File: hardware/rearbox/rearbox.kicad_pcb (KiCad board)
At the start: 4 copper layers, 120 x 60 mm, 7 parts

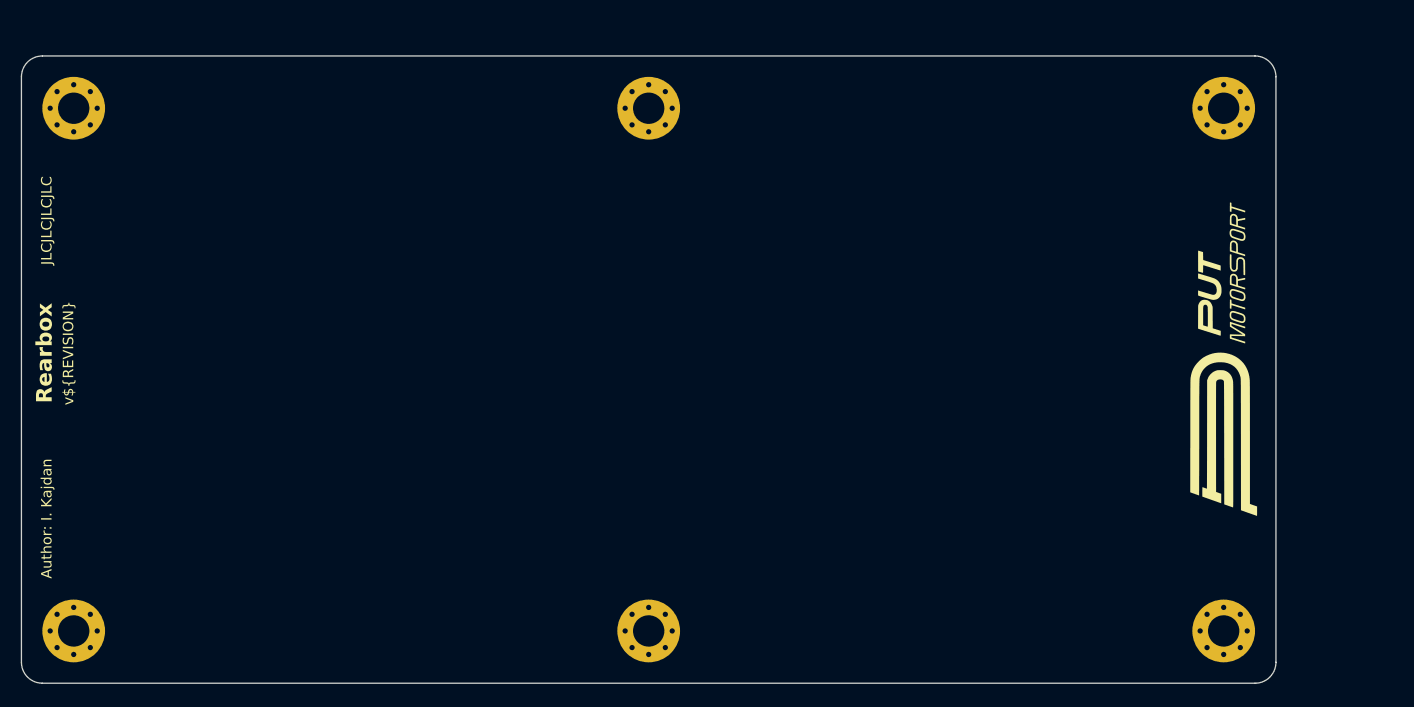
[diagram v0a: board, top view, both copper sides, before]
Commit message: Place components on the PCB
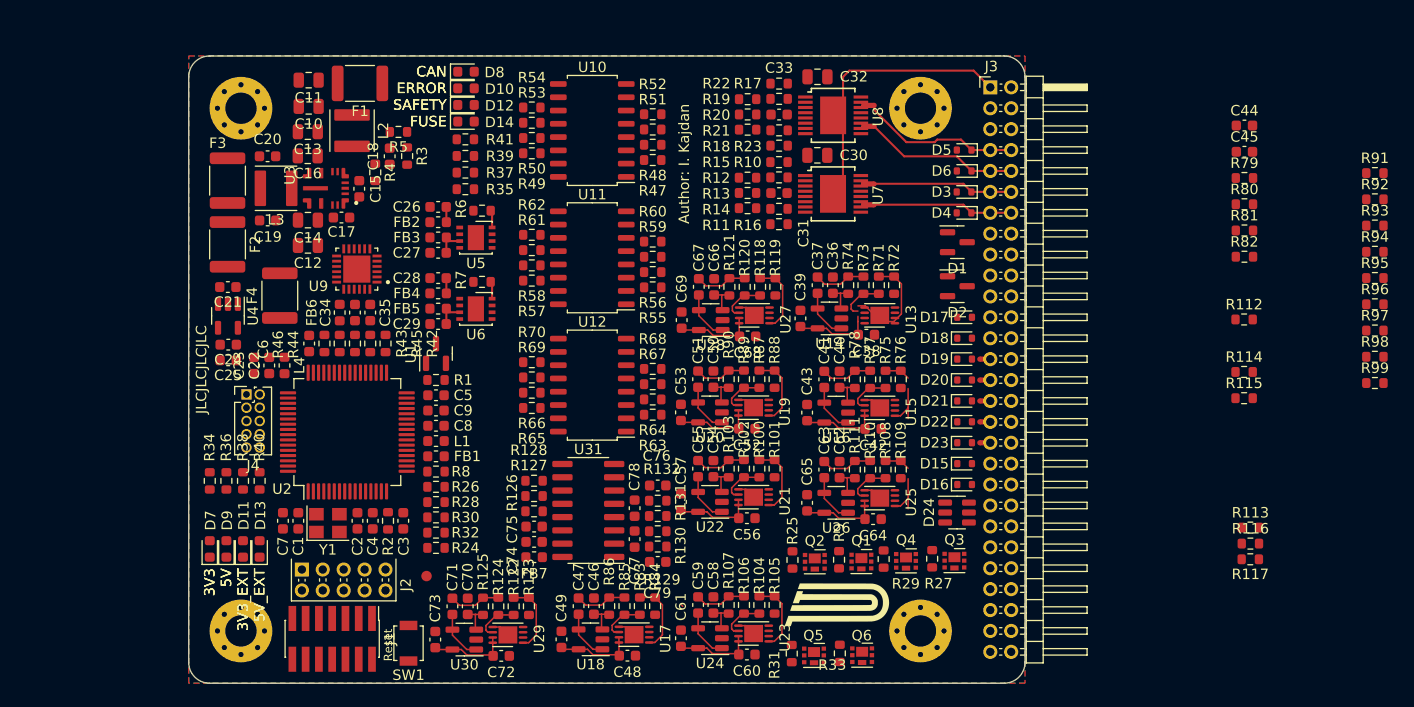
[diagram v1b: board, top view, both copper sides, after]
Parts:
- removed the REF** at (148.0, 129.0)
- removed the REF** at (148.0, 79.0)
- added C1: 10p, Capacitor_SMD:C_0603_1608Metric, F.Cu at (114.5, 118.5)
- added C10: 2u2, Capacitor_SMD:C_0805_2012Metric, F.Cu at (115.5, 78.8)
- added C11: 2u2, Capacitor_SMD:C_0805_2012Metric, F.Cu at (115.5, 76.3)
- added C12: 4u7, Capacitor_SMD:C_0805_2012Metric, F.Cu at (115.4, 92.1)
- added C13: 4u7, Capacitor_SMD:C_0805_2012Metric, F.Cu at (115.4, 81.2)
- added C14: 220n, Capacitor_SMD:C_0805_2012Metric, F.Cu at (115.4, 89.7)
- added C15: 1u, Capacitor_SMD:C_0603_1608Metric, F.Cu at (120.3, 86.7)
- added C16: 220n, Capacitor_SMD:C_0805_2012Metric, F.Cu at (115.4, 83.6)
- added C17: 100n, Capacitor_SMD:C_0603_1608Metric, F.Cu at (118.6, 89.5)
- added C18: 22p, Capacitor_SMD:C_0603_1608Metric, F.Cu at (123.2, 83.6)
- added C19: 22u, Capacitor_SMD:C_0603_1608Metric, F.Cu at (111.6, 89.7)
- added C2: 10p, Capacitor_SMD:C_0603_1608Metric, F.Cu at (120.1, 118.5)
- added C20: 22u, Capacitor_SMD:C_0603_1608Metric, F.Cu at (111.5, 83.6)
- added C21: 1u, Capacitor_SMD:C_0603_1608Metric, F.Cu at (107.7, 96.1)
- added C22: 1u, Capacitor_SMD:C_0603_1608Metric, F.Cu at (111.7, 103.6)
- added C23: 100n, Capacitor_SMD:C_0603_1608Metric, F.Cu at (110.2, 103.6)
- added C24: 100n, Capacitor_SMD:C_0603_1608Metric, F.Cu at (107.8, 101.6)
- added C25: 1u, Capacitor_SMD:C_0603_1608Metric, F.Cu at (107.8, 103.1)
- added C26: 100n, Capacitor_SMD:C_0603_1608Metric, F.Cu at (127.9, 88.4)
- added C27: 100n, Capacitor_SMD:C_0603_1608Metric, F.Cu at (127.9, 92.8)
- added C28: 100n, Capacitor_SMD:C_0603_1608Metric, F.Cu at (127.9, 95.2)
- added C29: 100n, Capacitor_SMD:C_0603_1608Metric, F.Cu at (127.9, 99.6)
- added C3: 100n, Capacitor_SMD:C_0603_1608Metric, F.Cu at (124.5, 118.5)
- added C30: 100n, Capacitor_SMD:C_0805_2012Metric, F.Cu at (164.1, 83.5)
- added C31: 10n, Capacitor_SMD:C_0603_1608Metric, F.Cu at (160.5, 87.1)
- added C32: 100n, Capacitor_SMD:C_0805_2012Metric, F.Cu at (164.1, 76.0)
- added C33: 10n, Capacitor_SMD:C_0603_1608Metric, F.Cu at (160.5, 79.6)
- added C34: 1u, Capacitor_SMD:C_0603_1608Metric, F.Cu at (119.9, 98.5)
- added C35: 100n, Capacitor_SMD:C_0603_1608Metric, F.Cu at (121.4, 98.5)
- added C36: 100n, Capacitor_SMD:C_0603_1608Metric, F.Cu at (165.6, 95.9)
- added C37: 100n, Capacitor_SMD:C_0603_1608Metric, F.Cu at (164.2, 95.9)
- added C38: 100n, Capacitor_SMD:C_0603_1608Metric, F.Cu at (168.8, 100.7)
- added C39: 100n, Capacitor_SMD:C_0603_1608Metric, F.Cu at (162.5, 99.1)
- added C4: 100n, Capacitor_SMD:C_0603_1608Metric, F.Cu at (121.6, 118.5)
- added C40: 100n, Capacitor_SMD:C_0603_1608Metric, F.Cu at (166.3, 104.9)
- added C41: 100n, Capacitor_SMD:C_0603_1608Metric, F.Cu at (164.8, 104.9)
- added C42: 100n, Capacitor_SMD:C_0603_1608Metric, F.Cu at (169.5, 109.7)
- added C43: 100n, Capacitor_SMD:C_0603_1608Metric, F.Cu at (163.2, 108.1)
- added C44: 10n, Capacitor_SMD:C_0603_1608Metric, F.Cu at (205.0, 80.7)
- added C45: 10n, Capacitor_SMD:C_0603_1608Metric, F.Cu at (205.0, 83.2)
- added C46: 100n, Capacitor_SMD:C_0603_1608Metric, F.Cu at (142.8, 126.6)
- added C47: 100n, Capacitor_SMD:C_0603_1608Metric, F.Cu at (141.3, 126.6)
- added C48: 100n, Capacitor_SMD:C_0603_1608Metric, F.Cu at (146.0, 131.4)
- added C49: 100n, Capacitor_SMD:C_0603_1608Metric, F.Cu at (139.7, 129.8)
- added C5: 100n, Capacitor_SMD:C_0603_1608Metric, F.Cu at (127.7, 106.5)
- added C50: 100n, Capacitor_SMD:C_0603_1608Metric, F.Cu at (154.2, 104.9)
- added C51: 100n, Capacitor_SMD:C_0603_1608Metric, F.Cu at (152.7, 104.9)
- added C52: 100n, Capacitor_SMD:C_0603_1608Metric, F.Cu at (157.4, 109.7)
- added C53: 100n, Capacitor_SMD:C_0603_1608Metric, F.Cu at (151.1, 108.1)
- added C54: 100n, Capacitor_SMD:C_0603_1608Metric, F.Cu at (154.2, 113.5)
- added C55: 100n, Capacitor_SMD:C_0603_1608Metric, F.Cu at (152.7, 113.5)
- added C56: 100n, Capacitor_SMD:C_0603_1608Metric, F.Cu at (157.4, 118.2)
- added C57: 100n, Capacitor_SMD:C_0603_1608Metric, F.Cu at (151.1, 116.7)
- added C58: 100n, Capacitor_SMD:C_0603_1608Metric, F.Cu at (154.2, 126.5)
- added C59: 100n, Capacitor_SMD:C_0603_1608Metric, F.Cu at (152.7, 126.5)
- added C6: 100n, Capacitor_SMD:C_0603_1608Metric, F.Cu at (115.5, 101.5)
- added C60: 100n, Capacitor_SMD:C_0603_1608Metric, F.Cu at (157.4, 131.3)
- added C61: 100n, Capacitor_SMD:C_0603_1608Metric, F.Cu at (151.1, 129.7)
- added C62: 100n, Capacitor_SMD:C_0603_1608Metric, F.Cu at (166.3, 113.6)
- added C63: 100n, Capacitor_SMD:C_0603_1608Metric, F.Cu at (164.8, 113.6)
- added C64: 100n, Capacitor_SMD:C_0603_1608Metric, F.Cu at (169.5, 118.3)
- added C65: 100n, Capacitor_SMD:C_0603_1608Metric, F.Cu at (163.2, 116.7)
- added C66: 100n, Capacitor_SMD:C_0603_1608Metric, F.Cu at (154.3, 96.1)
- added C67: 100n, Capacitor_SMD:C_0603_1608Metric, F.Cu at (152.8, 96.1)
- added C68: 100n, Capacitor_SMD:C_0603_1608Metric, F.Cu at (157.5, 100.8)
- added C69: 100n, Capacitor_SMD:C_0603_1608Metric, F.Cu at (151.2, 99.3)
- added C7: 100n, Capacitor_SMD:C_0603_1608Metric, F.Cu at (113.0, 118.5)
- added C70: 100n, Capacitor_SMD:C_0603_1608Metric, F.Cu at (130.7, 126.6)
- added C71: 100n, Capacitor_SMD:C_0603_1608Metric, F.Cu at (129.2, 126.6)
- added C72: 100n, Capacitor_SMD:C_0603_1608Metric, F.Cu at (133.9, 131.4)
- added C73: 100n, Capacitor_SMD:C_0603_1608Metric, F.Cu at (127.6, 129.8)
- added C74: 1u, Capacitor_SMD:C_0603_1608Metric, F.Cu at (137.0, 120.5)
- added C75: 100n, Capacitor_SMD:C_0603_1608Metric, F.Cu at (137.0, 119.0)
- added C76: 100n, Capacitor_SMD:C_0603_1608Metric, F.Cu at (148.9, 115.1)
- added C77: 100n, Capacitor_SMD:C_0603_1608Metric, F.Cu at (146.7, 120.2)
- added C78: 100n, Capacitor_SMD:C_0603_1608Metric, F.Cu at (146.7, 117.3)
- added C79: 1u, Capacitor_SMD:C_0603_1608Metric, F.Cu at (148.9, 122.4)
- added C8: 1u, Capacitor_SMD:C_0603_1608Metric, F.Cu at (127.7, 109.4)
- added C9: 100n, Capacitor_SMD:C_0603_1608Metric, F.Cu at (127.7, 107.9)
- added D1: PESD2CAN, Package_TO_SOT_SMD:SOT-23, F.Cu at (177.5, 91.8)
- added D10: Red, LED_SMD:LED_0603_1608Metric, F.Cu at (130.5, 77.1)
- added D11: Green, LED_SMD:LED_0603_1608Metric, F.Cu at (109.2, 121.2)
- added D12: Red, LED_SMD:LED_0603_1608Metric, F.Cu at (130.5, 78.7)
- added D13: Green, LED_SMD:LED_0603_1608Metric, F.Cu at (110.8, 121.2)
- added D14: Red, LED_SMD:LED_0603_1608Metric, F.Cu at (130.5, 80.3)
- added D15: 5V, Diode_SMD:D_SOD-523, F.Cu at (178.2, 113.0)
- added D16: 5V, Diode_SMD:D_SOD-523, F.Cu at (178.2, 115.0)
- added D17: 5V, Diode_SMD:D_SOD-523, F.Cu at (178.2, 99.0)
- added D18: 5V, Diode_SMD:D_SOD-523, F.Cu at (178.2, 101.0)
- added D19: 5V, Diode_SMD:D_SOD-523, F.Cu at (178.2, 103.0)
- added D2: PESD2CAN, Package_TO_SOT_SMD:SOT-23, F.Cu at (177.5, 96.0)
- added D20: 5V, Diode_SMD:D_SOD-523, F.Cu at (178.2, 105.0)
- added D21: 5V, Diode_SMD:D_SOD-523, F.Cu at (178.2, 107.0)
- added D22: 5V, Diode_SMD:D_SOD-523, F.Cu at (178.2, 109.0)
- added D23: 5V, Diode_SMD:D_SOD-523, F.Cu at (178.2, 111.0)
- added D24: CPDT6-5V4, Package_TO_SOT_SMD:SOT-23-6, F.Cu at (177.5, 117.7)
- added D3: PMEG3010EB, Diode_SMD:D_SOD-523, F.Cu at (178.2, 87.0)
- added D4: PMEG3010EB, Diode_SMD:D_SOD-523, F.Cu at (178.2, 89.0)
- added D5: PMEG3010EB, Diode_SMD:D_SOD-523, F.Cu at (178.2, 83.0)
- added D6: PMEG3010EB, Diode_SMD:D_SOD-523, F.Cu at (178.2, 85.0)
- added D7: Green, LED_SMD:LED_0603_1608Metric, F.Cu at (106.0, 121.2)
- added D8: Red, LED_SMD:LED_0603_1608Metric, F.Cu at (130.5, 75.5)
- added D9: Green, LED_SMD:LED_0603_1608Metric, F.Cu at (107.6, 121.2)
- added F1: 1.5A, Fuse:Fuse_1812_4532Metric, F.Cu at (120.4, 76.6)
- added F2: 500mA, Fuse:Fuse_1812_4532Metric, F.Cu at (107.7, 92.0)
- added F3: 200mA, Fuse:Fuse_1812_4532Metric, F.Cu at (107.7, 85.9)
- added F4: 100mA, Fuse:Fuse_1812_4532Metric, F.Cu at (112.7, 96.9)
- added FB1: 470R, Inductor_SMD:L_0603_1608Metric, F.Cu at (127.7, 112.3)
- added FB2: 470R, Inductor_SMD:L_0603_1608Metric, F.Cu at (127.9, 89.9)
- added FB3: 470R, Inductor_SMD:L_0603_1608Metric, F.Cu at (127.9, 91.4)
- added FB4: 470R, Inductor_SMD:L_0603_1608Metric, F.Cu at (127.9, 96.7)
- added FB5: 470R, Inductor_SMD:L_0603_1608Metric, F.Cu at (127.9, 98.2)
- added FB6: 470R, Inductor_SMD:L_0603_1608Metric, F.Cu at (118.4, 98.5)
- added FB7: 470R, Inductor_SMD:L_0603_1608Metric, F.Cu at (137.0, 121.9)
- added G***: LOGO, Local_Library:PUTM_Logo_10mm, F.Cu at (166.0, 126.5)
- added G***: LOGO, Local_Library:PUTM_Signature_Box_15mm, B.Cu at (152.4, 106.0)
- added J1: STDC14, Connector_PinHeader_1.27mm:PinHeader_2x07_P1.27mm_Vertical_SMD, F.Cu at (117.7, 129.8)
- added J2: ST-LINK, Local_Library:STLINK-V3MINIE, F.Cu at (114.8, 125.1)
- added J3: Conn_02x28_Top_Bottom, Connector_PinHeader_2.00mm:PinHeader_2x28_P2.00mm_Horizontal, F.Cu at (180.7, 77.0)
- added J4: Auxiliary, Connector_PinHeader_1.27mm:PinHeader_2x05_P1.27mm_Vertical, F.Cu at (109.5, 106.4)
- added L1: 10u, Inductor_SMD:L_0603_1608Metric, F.Cu at (127.7, 110.8)
- added L2: 1u5, Inductor_SMD:L_Abracon_ASPI-4030S, F.Cu at (119.6, 81.1)
- added L3: 1u5, Inductor_SMD:L_Abracon_ASPI-4030S, F.Cu at (112.4, 86.7)
- added L4: 10u, Inductor_SMD:L_0603_1608Metric, F.Cu at (113.2, 103.6)
- added NT1: NetTie_2, NetTie:NetTie-2_SMD_Pad0.5mm, F.Cu at (169.1, 86.2)
- added NT2: NetTie_2, NetTie:NetTie-2_SMD_Pad0.5mm, F.Cu at (169.1, 88.2)
- added NT3: NetTie_2, NetTie:NetTie-2_SMD_Pad0.5mm, F.Cu at (169.1, 78.7)
- added NT4: NetTie_2, NetTie:NetTie-2_SMD_Pad0.5mm, F.Cu at (169.1, 80.7)
- added NT5: NetTie_2, NetTie:NetTie-2_SMD_Pad0.5mm, F.Cu at (180.2, 103.0)
- added NT6: NetTie_2, NetTie:NetTie-2_SMD_Pad0.5mm, F.Cu at (180.2, 105.0)
- added NT7: NetTie_2, NetTie:NetTie-2_SMD_Pad0.5mm, F.Cu at (180.2, 107.0)
- added NT8: NetTie_2, NetTie:NetTie-2_SMD_Pad0.5mm, F.Cu at (180.2, 109.0)
- added NT9: NetTie_2, NetTie:NetTie-2_SMD_Pad0.5mm, F.Cu at (180.2, 111.0)
- added Q1: BUK6D210, Package_DFN_QFN:Diodes_UDFN2020-6_Type-F, F.Cu at (168.3, 122.4)
- added Q2: BUK6D210, Package_DFN_QFN:Diodes_UDFN2020-6_Type-F, F.Cu at (163.9, 122.4)
- added Q3: BUK6D210, Package_DFN_QFN:Diodes_UDFN2020-6_Type-F, F.Cu at (177.2, 122.3)
- added Q4: BUK6D210, Package_DFN_QFN:Diodes_UDFN2020-6_Type-F, F.Cu at (172.6, 122.3)
- added Q5: BUK6D210, Package_DFN_QFN:Diodes_UDFN2020-6_Type-F, F.Cu at (163.8, 131.3)
- added Q6: BUK6D210, Package_DFN_QFN:Diodes_UDFN2020-6_Type-F, F.Cu at (168.4, 131.3)
- added R1: 1k, Resistor_SMD:R_0603_1608Metric, F.Cu at (127.7, 105.0)
- added R10: 100R, Resistor_SMD:R_0603_1608Metric, F.Cu at (160.5, 84.2)
- added R100: TBD, Resistor_SMD:R_0603_1608Metric, F.Cu at (158.6, 113.5)
- added R101: TBD, Resistor_SMD:R_0603_1608Metric, F.Cu at (160.0, 113.5)
- added R102: 3k3, Resistor_SMD:R_0603_1608Metric, F.Cu at (157.1, 113.5)
- added R103: 3k3, Resistor_SMD:R_0603_1608Metric, F.Cu at (155.7, 113.5)
- added R104: TBD, Resistor_SMD:R_0603_1608Metric, F.Cu at (158.6, 126.5)
- added R105: TBD, Resistor_SMD:R_0603_1608Metric, F.Cu at (160.0, 126.5)
- added R106: 3k3, Resistor_SMD:R_0603_1608Metric, F.Cu at (157.1, 126.5)
- added R107: 3k3, Resistor_SMD:R_0603_1608Metric, F.Cu at (155.7, 126.5)
- added R108: TBD, Resistor_SMD:R_0603_1608Metric, F.Cu at (170.7, 113.6)
- added R109: TBD, Resistor_SMD:R_0603_1608Metric, F.Cu at (172.1, 113.6)
- added R11: 100R, Resistor_SMD:R_0603_1608Metric, F.Cu at (160.5, 90.1)
- added R110: 3k3, Resistor_SMD:R_0603_1608Metric, F.Cu at (169.2, 113.6)
- added R111: 3k3, Resistor_SMD:R_0603_1608Metric, F.Cu at (167.7, 113.6)
- added R112: 50k, Resistor_SMD:R_0603_1608Metric, F.Cu at (205.0, 99.2)
- added R113: 50k, Resistor_SMD:R_0603_1608Metric, F.Cu at (205.6, 119.1)
- added R114: 50k, Resistor_SMD:R_0603_1608Metric, F.Cu at (205.0, 104.2)
- added R115: 5k, Resistor_SMD:R_0603_1608Metric, F.Cu at (205.0, 106.7)
- added R116: 50k, Resistor_SMD:R_0603_1608Metric, F.Cu at (205.6, 120.6)
- added R117: 5k, Resistor_SMD:R_0603_1608Metric, F.Cu at (205.5, 122.1)
- added R118: TBD, Resistor_SMD:R_0603_1608Metric, F.Cu at (158.7, 96.1)
- added R119: TBD, Resistor_SMD:R_0603_1608Metric, F.Cu at (160.1, 96.1)
- added R12: 100R, Resistor_SMD:R_0603_1608Metric, F.Cu at (157.5, 85.6)
- added R120: 3k3, Resistor_SMD:R_0603_1608Metric, F.Cu at (157.2, 96.1)
- added R121: 3k3, Resistor_SMD:R_0603_1608Metric, F.Cu at (155.7, 96.1)
- added R122: TBD, Resistor_SMD:R_0603_1608Metric, F.Cu at (135.1, 126.6)
- added R123: TBD, Resistor_SMD:R_0603_1608Metric, F.Cu at (136.5, 126.6)
- added R124: 3k3, Resistor_SMD:R_0603_1608Metric, F.Cu at (133.6, 126.6)
- added R125: 3k3, Resistor_SMD:R_0603_1608Metric, F.Cu at (132.2, 126.6)
- added R126: 100R, Resistor_SMD:R_0603_1608Metric, F.Cu at (137.0, 117.6)
- added R127: 100R, Resistor_SMD:R_0603_1608Metric, F.Cu at (137.0, 116.1)
- added R128: 100R, Resistor_SMD:R_0603_1608Metric, F.Cu at (137.0, 114.6)
- added R129: 51R, Resistor_SMD:R_0603_1608Metric, F.Cu at (148.9, 120.9)
- added R13: 100R, Resistor_SMD:R_0603_1608Metric, F.Cu at (157.5, 87.1)
- added R130: 51R, Resistor_SMD:R_0603_1608Metric, F.Cu at (148.9, 119.5)
- added R131: 51R, Resistor_SMD:R_0603_1608Metric, F.Cu at (148.9, 118.0)
- added R132: 51R, Resistor_SMD:R_0603_1608Metric, F.Cu at (148.9, 116.5)
- added R14: 100R, Resistor_SMD:R_0603_1608Metric, F.Cu at (157.5, 88.6)
- added R15: 15k, Resistor_SMD:R_0603_1608Metric, F.Cu at (160.5, 85.6)
- added R16: TBD, Resistor_SMD:R_0603_1608Metric, F.Cu at (160.5, 88.6)
- added R17: 100R, Resistor_SMD:R_0603_1608Metric, F.Cu at (160.5, 76.6)
- added R18: 100R, Resistor_SMD:R_0603_1608Metric, F.Cu at (160.5, 82.6)
- added R19: 100R, Resistor_SMD:R_0603_1608Metric, F.Cu at (157.5, 78.1)
- added R2: 10k, Resistor_SMD:R_0603_1608Metric, F.Cu at (123.1, 118.5)
- added R20: 100R, Resistor_SMD:R_0603_1608Metric, F.Cu at (157.5, 79.6)
- added R21: 100R, Resistor_SMD:R_0603_1608Metric, F.Cu at (157.5, 81.0)
- added R22: 15k, Resistor_SMD:R_0603_1608Metric, F.Cu at (160.5, 78.1)
- added R23: TBD, Resistor_SMD:R_0603_1608Metric, F.Cu at (160.5, 81.1)
- added R24: 100R, Resistor_SMD:R_0603_1608Metric, F.Cu at (127.7, 121.1)
- added R25: 10k, Resistor_SMD:R_0603_1608Metric, F.Cu at (161.8, 122.2)
- added R26: 100R, Resistor_SMD:R_0603_1608Metric, F.Cu at (127.7, 115.2)
- added R27: 10k, Resistor_SMD:R_0603_1608Metric, F.Cu at (175.1, 122.1)
- added R28: 100R, Resistor_SMD:R_0603_1608Metric, F.Cu at (127.7, 116.7)
- added R29: 10k, Resistor_SMD:R_0603_1608Metric, F.Cu at (170.5, 122.1)
- added R3: 100k, Resistor_SMD:R_0603_1608Metric, F.Cu at (124.9, 83.6)
- added R30: 100R, Resistor_SMD:R_0603_1608Metric, F.Cu at (127.7, 118.1)
- added R31: 10k, Resistor_SMD:R_0603_1608Metric, F.Cu at (161.7, 131.2)
- added R32: 100R, Resistor_SMD:R_0603_1608Metric, F.Cu at (127.7, 119.6)
- added R33: 10k, Resistor_SMD:R_0603_1608Metric, F.Cu at (166.3, 131.1)
- added R34: 82R, Resistor_SMD:R_0603_1608Metric, F.Cu at (106.0, 114.6)
- added R35: 120R, Resistor_SMD:R_0603_1608Metric, F.Cu at (130.5, 86.7)
- added R36: 270R, Resistor_SMD:R_0603_1608Metric, F.Cu at (107.6, 114.6)
- added R37: 120R, Resistor_SMD:R_0603_1608Metric, F.Cu at (130.5, 85.2)
- added R38: 82R, Resistor_SMD:R_0603_1608Metric, F.Cu at (109.2, 114.6)
- added R39: 120R, Resistor_SMD:R_0603_1608Metric, F.Cu at (130.5, 83.6)
- added R4: 24k9, Resistor_SMD:R_0603_1608Metric, F.Cu at (121.8, 85.1)
- added R40: 270R, Resistor_SMD:R_0603_1608Metric, F.Cu at (110.8, 114.6)
- added R41: 120R, Resistor_SMD:R_0603_1608Metric, F.Cu at (130.5, 82.0)
- added R42: 100R, Resistor_SMD:R_0603_1608Metric, F.Cu at (122.8, 101.5)
- added R43: 100R, Resistor_SMD:R_0603_1608Metric, F.Cu at (119.9, 101.5)
- added R44: 100R, Resistor_SMD:R_0603_1608Metric, F.Cu at (118.4, 101.5)
- added R45: 100R, Resistor_SMD:R_0603_1608Metric, F.Cu at (121.4, 101.5)
- added R46: 0R, Resistor_SMD:R_0603_1608Metric, F.Cu at (117.0, 101.5)
- added R47: 2k, Resistor_SMD:R_0603_1608Metric, F.Cu at (148.4, 84.0)
- added R48: 2k, Resistor_SMD:R_0603_1608Metric, F.Cu at (148.4, 82.5)
- added R49: 10k, Resistor_SMD:R_0603_1608Metric, F.Cu at (136.8, 83.3)
- added R5: 1k, Resistor_SMD:R_0603_1608Metric, F.Cu at (124.1, 81.3)
- added R50: 10k, Resistor_SMD:R_0603_1608Metric, F.Cu at (136.8, 81.8)
- added R51: 2k, Resistor_SMD:R_0603_1608Metric, F.Cu at (148.4, 81.0)
- added R52: 2k, Resistor_SMD:R_0603_1608Metric, F.Cu at (148.4, 79.6)
- added R53: 10k, Resistor_SMD:R_0603_1608Metric, F.Cu at (136.8, 80.4)
- added R54: 10k, Resistor_SMD:R_0603_1608Metric, F.Cu at (136.8, 78.9)
- added R55: 2k, Resistor_SMD:R_0603_1608Metric, F.Cu at (148.4, 96.1)
- added R56: 2k, Resistor_SMD:R_0603_1608Metric, F.Cu at (148.4, 94.7)
- added R57: 10k, Resistor_SMD:R_0603_1608Metric, F.Cu at (136.8, 95.5)
- added R58: 10k, Resistor_SMD:R_0603_1608Metric, F.Cu at (136.8, 94.0)
- added R59: 2k, Resistor_SMD:R_0603_1608Metric, F.Cu at (148.4, 93.2)
- added R6: 0R, Resistor_SMD:R_0603_1608Metric, F.Cu at (132.1, 88.8)
- added R60: 2k, Resistor_SMD:R_0603_1608Metric, F.Cu at (148.4, 91.8)
- added R61: 10k, Resistor_SMD:R_0603_1608Metric, F.Cu at (136.8, 92.6)
- added R62: 10k, Resistor_SMD:R_0603_1608Metric, F.Cu at (136.8, 91.1)
- added R63: 2k, Resistor_SMD:R_0603_1608Metric, F.Cu at (148.4, 108.3)
- added R64: 2k, Resistor_SMD:R_0603_1608Metric, F.Cu at (148.4, 106.9)
- added R65: 10k, Resistor_SMD:R_0603_1608Metric, F.Cu at (136.8, 107.7)
- added R66: 10k, Resistor_SMD:R_0603_1608Metric, F.Cu at (136.8, 106.2)
- added R67: 2k, Resistor_SMD:R_0603_1608Metric, F.Cu at (148.4, 105.4)
- added R68: 2k, Resistor_SMD:R_0603_1608Metric, F.Cu at (148.4, 103.9)
- added R69: 10k, Resistor_SMD:R_0603_1608Metric, F.Cu at (136.8, 104.8)
- added R7: 0R, Resistor_SMD:R_0603_1608Metric, F.Cu at (132.1, 95.6)
- added R70: 10k, Resistor_SMD:R_0603_1608Metric, F.Cu at (136.8, 103.3)
- added R71: TBD, Resistor_SMD:R_0603_1608Metric, F.Cu at (170.0, 95.9)
- added R72: TBD, Resistor_SMD:R_0603_1608Metric, F.Cu at (171.5, 95.9)
- added R73: 3k3, Resistor_SMD:R_0603_1608Metric, F.Cu at (168.5, 95.9)
- added R74: 3k3, Resistor_SMD:R_0603_1608Metric, F.Cu at (167.1, 95.9)
- added R75: TBD, Resistor_SMD:R_0603_1608Metric, F.Cu at (170.7, 104.9)
- added R76: TBD, Resistor_SMD:R_0603_1608Metric, F.Cu at (172.1, 104.9)
- added R77: 3k3, Resistor_SMD:R_0603_1608Metric, F.Cu at (169.2, 104.9)
- added R78: 3k3, Resistor_SMD:R_0603_1608Metric, F.Cu at (167.7, 104.9)
- added R79: 560R, Resistor_SMD:R_0603_1608Metric, F.Cu at (205.0, 85.7)
- added R8: 100R, Resistor_SMD:R_0603_1608Metric, F.Cu at (127.7, 113.8)
- added R80: 100R, Resistor_SMD:R_0603_1608Metric, F.Cu at (205.0, 88.2)
- added R81: 560R, Resistor_SMD:R_0603_1608Metric, F.Cu at (205.0, 90.7)
- added R82: 100R, Resistor_SMD:R_0603_1608Metric, F.Cu at (205.0, 93.2)
- added R83: TBD, Resistor_SMD:R_0603_1608Metric, F.Cu at (147.2, 126.6)
- added R84: TBD, Resistor_SMD:R_0603_1608Metric, F.Cu at (148.6, 126.6)
- added R85: 3k3, Resistor_SMD:R_0603_1608Metric, F.Cu at (145.7, 126.6)
- added R86: 3k3, Resistor_SMD:R_0603_1608Metric, F.Cu at (144.2, 126.6)
- added R87: TBD, Resistor_SMD:R_0603_1608Metric, F.Cu at (158.6, 104.9)
- added R88: TBD, Resistor_SMD:R_0603_1608Metric, F.Cu at (160.0, 104.9)
- added R89: 3k3, Resistor_SMD:R_0603_1608Metric, F.Cu at (157.1, 104.9)
- added R9: 10k, Resistor_SMD:R_0603_1608Metric, F.Cu at (166.2, 122.2)
- added R90: 3k3, Resistor_SMD:R_0603_1608Metric, F.Cu at (155.7, 104.9)
- added R91: 1k, Resistor_SMD:R_0603_1608Metric, F.Cu at (217.5, 85.2)
- added R92: 1k, Resistor_SMD:R_0603_1608Metric, F.Cu at (217.5, 87.7)
- added R93: 1k, Resistor_SMD:R_0603_1608Metric, F.Cu at (217.5, 90.2)
- added R94: 1k, Resistor_SMD:R_0603_1608Metric, F.Cu at (217.5, 92.7)
- added R95: 3k, Resistor_SMD:R_0603_1608Metric, F.Cu at (217.5, 95.2)
- added R96: 1k, Resistor_SMD:R_0603_1608Metric, F.Cu at (217.5, 97.8)
- added R97: 3k, Resistor_SMD:R_0603_1608Metric, F.Cu at (217.5, 100.3)
- added R98: 1k, Resistor_SMD:R_0603_1608Metric, F.Cu at (217.5, 102.8)
- added R99: 3k, Resistor_SMD:R_0603_1608Metric, F.Cu at (217.5, 105.3)
- added REF**: Fiducial_1mm_Mask2mm, Fiducial:Fiducial_1mm_Mask2mm, F.Cu at (126.8, 123.8)
- added SW1: Reset, Button_Switch_SMD:SW_SPST_B3U-1000P, F.Cu at (125.0, 130.2)
- added U1: LM4040C33FTA, Package_TO_SOT_SMD:SOT-23, F.Cu at (127.7, 102.5)
- added U10: TLP291-4, Package_SO:SOIC-16_4.55x10.3mm_P1.27mm, F.Cu at (142.6, 81.1)
- added U11: TLP291-4, Package_SO:SOIC-16_4.55x10.3mm_P1.27mm, F.Cu at (142.6, 93.3)
- added U12: TLP291-4, Package_SO:SOIC-16_4.55x10.3mm_P1.27mm, F.Cu at (142.6, 105.5)
- added U13: MCP6N11-005, Package_DFN_QFN:TDFN-8-1EP_3x2mm_P0.5mm_EP1.80x1.65mm, F.Cu at (170.1, 98.8)
- added U14: MCP6001, Package_TO_SOT_SMD:SOT-23-5, F.Cu at (165.3, 99.1)
- added U15: MCP6N11-005, Package_DFN_QFN:TDFN-8-1EP_3x2mm_P0.5mm_EP1.80x1.65mm, F.Cu at (170.1, 107.7)
- added U16: MCP6001, Package_TO_SOT_SMD:SOT-23-5, F.Cu at (165.9, 108.1)
- added U17: MCP6N11-005, Package_DFN_QFN:TDFN-8-1EP_3x2mm_P0.5mm_EP1.80x1.65mm, F.Cu at (146.6, 129.4)
- added U18: MCP6001, Package_TO_SOT_SMD:SOT-23-5, F.Cu at (142.4, 129.8)
- added U19: MCP6N11-005, Package_DFN_QFN:TDFN-8-1EP_3x2mm_P0.5mm_EP1.80x1.65mm, F.Cu at (158.0, 107.6)
- added U2: STM32G473RCTx, Package_QFP:LQFP-64_10x10mm_P0.5mm, F.Cu at (119.2, 110.0)
- added U20: MCP6001, Package_TO_SOT_SMD:SOT-23-5, F.Cu at (153.9, 108.1)
- added U21: MCP6N11-005, Package_DFN_QFN:TDFN-8-1EP_3x2mm_P0.5mm_EP1.80x1.65mm, F.Cu at (158.0, 116.2)
- added U22: MCP6001, Package_TO_SOT_SMD:SOT-23-5, F.Cu at (153.9, 116.7)
- added U23: MCP6N11-005, Package_DFN_QFN:TDFN-8-1EP_3x2mm_P0.5mm_EP1.80x1.65mm, F.Cu at (158.0, 129.2)
- added U24: MCP6001, Package_TO_SOT_SMD:SOT-23-5, F.Cu at (153.9, 129.7)
- added U25: MCP6N11-005, Package_DFN_QFN:TDFN-8-1EP_3x2mm_P0.5mm_EP1.80x1.65mm, F.Cu at (170.1, 116.3)
- added U26: MCP6001, Package_TO_SOT_SMD:SOT-23-5, F.Cu at (165.9, 116.7)
- added U27: MCP6N11-005, Package_DFN_QFN:TDFN-8-1EP_3x2mm_P0.5mm_EP1.80x1.65mm, F.Cu at (158.1, 98.8)
- added U28: MCP6001, Package_TO_SOT_SMD:SOT-23-5, F.Cu at (153.9, 99.3)
- added U29: MCP6N11-005, Package_DFN_QFN:TDFN-8-1EP_3x2mm_P0.5mm_EP1.80x1.65mm, F.Cu at (134.5, 129.4)
- added U3: LM62440-Q1, Local_Library:IC_LM61460AANRJRR, F.Cu at (117.1, 86.7)
- added U30: MCP6001, Package_TO_SOT_SMD:SOT-23-5, F.Cu at (130.4, 129.8)
- added U31: NAU7802SGI, Package_SO:SOIC-16_3.9x9.9mm_P1.27mm, F.Cu at (142.2, 117.5)
- added U4: TLV743P, Package_TO_SOT_SMD:SOT-23-5, F.Cu at (107.8, 98.9)
- added U5: MCP2542FD, Package_DFN_QFN:DFN-8-1EP_3x3mm_P0.65mm_EP1.55x2.4mm, F.Cu at (131.5, 91.4)
- added U6: MCP2542FD, Package_DFN_QFN:DFN-8-1EP_3x3mm_P0.65mm_EP1.55x2.4mm, F.Cu at (131.5, 98.2)
- added U7: VND7020AJTR, Local_Library:VND7020AJTR, F.Cu at (165.6, 87.2)
- added U8: VND7020AJTR, Local_Library:VND7020AJTR, F.Cu at (165.6, 79.7)
- added U9: TCA6416ARTWR, Local_Library:QFN50P400X400X80-25N, F.Cu at (120.1, 94.4)
- added Y1: 48MHz, Crystal:Crystal_SMD_Abracon_ABM8G-4Pin_3.2x2.5mm, F.Cu at (117.3, 118.7)
- G***: moved to B.Cu
- moved G*** 29.2 mm to (173.8, 103.0)
- moved REF** 29.0 mm to (174.0, 79.0)
- moved REF** 29.0 mm to (174.0, 129.0)
- moved REF** 16.0 mm to (109.0, 129.0)
- moved REF** 16.0 mm to (109.0, 79.0)
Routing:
- net +3.3VA: track 0.00 -> 68.7 mm
- net +24V: track 0.00 -> 27.4 mm
- net GND: track 0.00 -> 15.8 mm
- net PUMP_OUT1: track 0.00 -> 15.3 mm
- net PUMP_OUT2: track 0.00 -> 14.9 mm
- net FAN_OUT_R: track 0.00 -> 13.4 mm
- net FAN_OUT_L: track 0.00 -> 13.4 mm
- net Net-(U13-FG): track 0.00 -> 6.89 mm
- net Net-(U27-FG): track 0.00 -> 6.89 mm
- net Net-(U25-FG): track 0.00 -> 6.89 mm
- net Net-(U15-FG): track 0.00 -> 6.89 mm
- net Net-(U17-FG): track 0.00 -> 6.89 mm
- net Net-(U29-FG): track 0.00 -> 6.89 mm
- net Net-(U23-FG): track 0.00 -> 6.89 mm
- net Net-(U21-FG): track 0.00 -> 6.89 mm
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- added copper zone on B.Cu, net GND
- added copper zone on F.Cu, net GND
- added copper zone on In1.Cu, net GND
- added copper zone on In2.Cu, net GND
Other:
- board size 120 x 60 mm -> 80 x 60 mm
- board text added: "3V3"
- board text added: "3V3_EXT"
- board text added: "5V"
- board text added: "5V_EXT"
- board text added: "CAN"
- board text added: "ERROR"
- board text added: "FUSE"
- board text added: "Reset"
- board text added: "SAFETY"

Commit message: Align footprint references
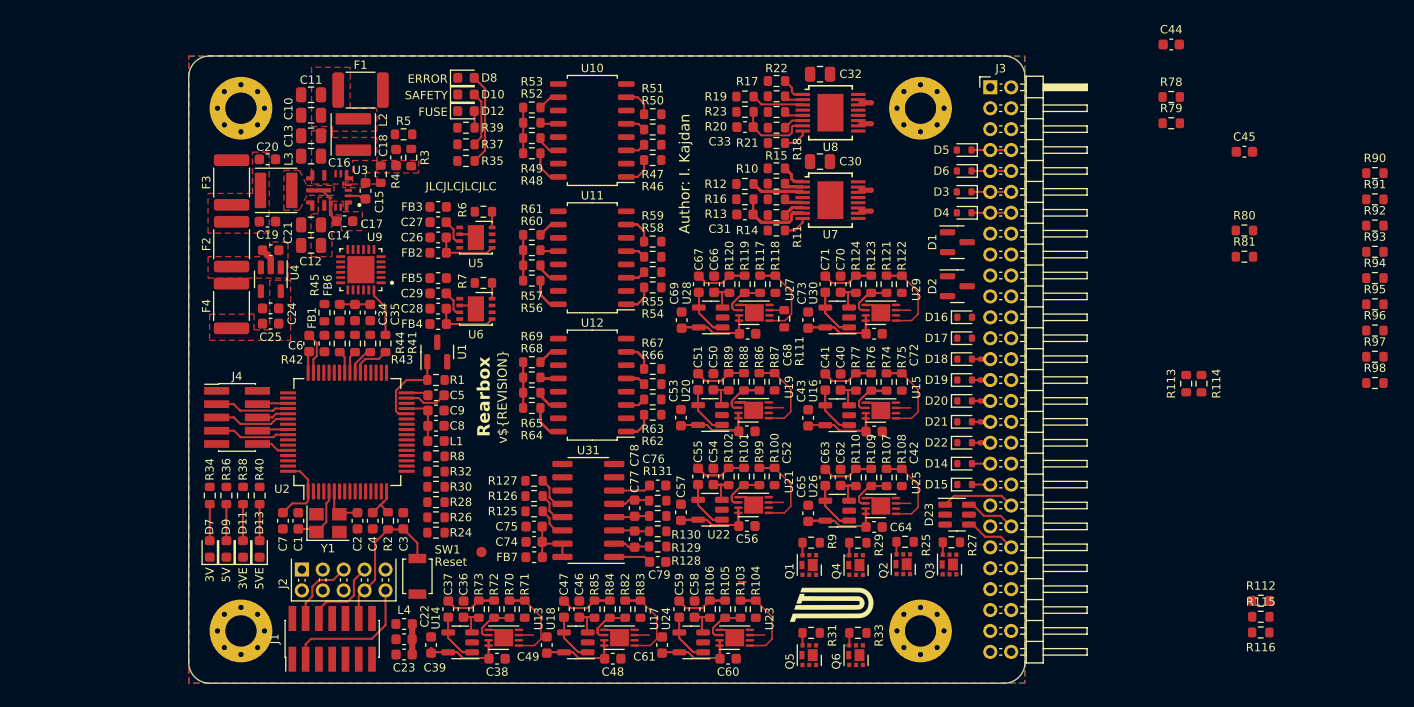
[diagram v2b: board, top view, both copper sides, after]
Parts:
- removed the D8 at (130.5, 75.5)
- removed the G*** at (166.0, 126.5)
- removed the R35 at (130.5, 86.7)
- added G***: LOGO, Local_Library:PUTM_Logo_8mm, F.Cu at (165.5, 126.5)
- J4: footprint Connector_PinHeader_1.27mm:PinHeader_2x05_P1.27mm_Vertical -> Connector_PinHeader_1.27mm:PinHeader_2x05_P1.27mm_Vertical_SMD
- moved U13 47.4 mm to (134.1, 129.6)
- moved C39 47.2 mm to (127.2, 130.3)
- moved C70 47.1 mm to (166.4, 95.8)
- moved C71 47.1 mm to (164.9, 95.8)
- moved R122 47.1 mm to (172.2, 95.8)
- moved U29 47.1 mm to (170.2, 98.6)
- moved R121 47.1 mm to (170.8, 95.8)
- moved R123 47.1 mm to (169.3, 95.8)
- moved R124 47.1 mm to (167.8, 95.8)
- moved C72 47.1 mm to (169.6, 100.6)
- moved U30 47.1 mm to (166.0, 99.0)
- moved C36 47.0 mm to (130.3, 126.9)
- moved C37 47.0 mm to (128.8, 126.9)
- moved R73 47.0 mm to (131.8, 126.9)
- moved C38 47.0 mm to (133.5, 131.7)
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- renumbered D12 to D10, D14 to D12, D15 to D14, D16 to D15, D17 to D16, D18 to D17, D19 to D18, D20 to D19, D21 to D20, D22 to D21, D23 to D22, D24 to D23, D10 to D8, R101 to R100, R102 to R101, R103 to R102, R104 to R103, R105 to R104, R106 to R105, R107 to R106, R108 to R107, R109 to R108, R110 to R109, R111 to R110, R112 to R111, R113 to R112, R114 to R113, R115 to R114, R116 to R115, R117 to R116, R118 to R117, R119 to R118, R120 to R119, R121 to R120, R122 to R121, R123 to R122, R124 to R123, R125 to R124, R126 to R125, R127 to R126, R128 to R127, R129 to R128, R130 to R129, R131 to R130, R132 to R131, R37 to R35, R39 to R37, R41 to R39, R42 to R41, R43 to R42, R44 to R43, R45 to R44, R46 to R45, R47 to R46, R48 to R47, R49 to R48, R50 to R49, R51 to R50, R52 to R51, R53 to R52, R54 to R53, R55 to R54, R56 to R55, R57 to R56, R58 to R57, R59 to R58, R60 to R59, R61 to R60, R62 to R61, R63 to R62, R64 to R63, R65 to R64, R66 to R65, R67 to R66, R68 to R67, R69 to R68, R70 to R69, R71 to R70, R72 to R71, R73 to R72, R74 to R73, R75 to R74, R76 to R75, R77 to R76, R78 to R77, R79 to R78, R80 to R79, R81 to R80, R82 to R81, R83 to R82, R84 to R83, R85 to R84, R86 to R85, R87 to R86, R88 to R87, R89 to R88, R90 to R89, R91 to R90, R92 to R91, R93 to R92, R94 to R93, R95 to R94, R96 to R95, R97 to R96, R98 to R97, R99 to R98, R100 to R99
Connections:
- net Net-(C10-Pad1) renamed /Power Supply/+24V_FUSED
- net Net-(U4-EN) renamed /Power Supply/+5V_FUSED
- J3 pad 42: ASSI_OUT_R -> LOAD_CELL_IN_L+
- J3 pad 43: LOAD_CELL_IN_L+ -> ASSI_OUT_R
- J3 pad 44: ASSI_OUT_G -> LOAD_CELL_IN_L-
- J3 pad 45: LOAD_CELL_IN_L- -> ASSI_OUT_G
- J3 pad 46: ASSI_OUT_B -> LOAD_CELL_IN_R+
- J3 pad 47: LOAD_CELL_IN_R+ -> ASSI_OUT_B
- J3 pad 48: BRAKE_LIGHT_OUT -> LOAD_CELL_IN_R-
- J3 pad 49: LOAD_CELL_IN_R- -> BRAKE_LIGHT_OUT
- J3 pad 50: ASSI_OUT_BUZZER -> GND
- J3 pad 52: RTDS_OUT -> GND
- J3 pad 53: GND -> ASSI_OUT_BUZZER
- J3 pad 55: GND -> RTDS_OUT
- J4 pad 5: UART_RX -> SPI_MOSI
- J4 pad 6: SPI_MOSI -> UART_RX
- J4 pad 7: SPI_SCLK -> SPI_MISO
- J4 pad 8: SPI_MISO -> SPI_SCLK
- U2 pad 11: /WATER_PRESSURE1 -> /WATER_TEMPERATURE1
- U2 pad 12: /WATER_PRESSURE2 -> /WATER_TEMPERATURE2
- U2 pad 13: /POTENTIOMETER_L -> /WATER_PRESSURE1
- U2 pad 14: /POTENTIOMETER_R -> /WATER_PRESSURE2
- U2 pad 17: unconnected-(U2-PA3-Pad17) -> /ASSI_LED_B
- U2 pad 2: /ASSI_LED_R -> /BRAKE_LIGHT
- U2 pad 22: /SENSE_OUT -> /POTENTIOMETER_L
- U2 pad 23: /SENSE_ADDRESS_IN1 -> /POTENTIOMETER_R
- U2 pad 24: /SENSE_ADDRESS_IN0 -> /SENSE_OUT
- U2 pad 25: /SENSE_ENABLE_PUMPS -> /SENSE_ADDRESS_IN0
- U2 pad 26: /SENSE_ENABLE_FANS -> /SENSE_ADDRESS_IN1
- U2 pad 3: /ASSI_LED_G -> /RTDS
- U2 pad 33: unconnected-(U2-PB11-Pad33) -> /PUMP1
- U2 pad 34: unconnected-(U2-PB12-Pad34) -> /CAN2_RX
- U2 pad 35: /PUMP1 -> /CAN2_TX
- U2 pad 4: /ASSI_LED_B -> /ASSI_BUZZER
- U2 pad 45: /RTDS -> /CAN_RX
- U2 pad 46: /ASSI_BUZZER -> /CAN_TX
- U2 pad 55: /BRAKE_LIGHT -> unconnected-(U2-PD2-Pad55)
- U2 pad 58: /CAN2_RX -> /SENSE_ENABLE_PUMPS
- U2 pad 59: /CAN2_TX -> /SENSE_ENABLE_FANS
- U2 pad 61: /CAN_RX -> unconnected-(U2-PB8-Pad61)
- U2 pad 62: /CAN_TX -> unconnected-(U2-PB9-Pad62)
- U2 pad 8: /WATER_TEMPERATURE1 -> /ASSI_LED_R
- U2 pad 9: /WATER_TEMPERATURE2 -> /ASSI_LED_G
- U9 pad 5: /LED_CAN -> unconnected-(U9-P04-Pad5)
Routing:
- net +3.3VA: track 68.7 -> 209.8 mm
- net GND: track 15.8 -> 62.3 mm
- net /SENSE_OUT: track 0.00 -> 43.3 mm
- net VDD: track 0.00 -> 28.1 mm
- net +24V: track 27.4 -> 0.00 mm
- net Net-(U7-SEn): track 0.00 -> 25.1 mm
- net +3.3V: track 0.00 -> 21.9 mm
- net NRST: track 0.00 -> 14.5 mm
- net Net-(U7-INPUT0): track 0.00 -> 12.3 mm
- net PUMP_OUT1: track 15.3 -> 3.80 mm
- net PUMP_OUT2: track 14.9 -> 3.80 mm
- net Net-(C37-Pad1): track 4.97 -> 14.9 mm
- net Net-(C67-Pad1): track 4.97 -> 14.9 mm
- net Net-(C55-Pad1): track 4.97 -> 14.9 mm
- net Net-(C51-Pad1): track 4.97 -> 14.9 mm
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- added copper zone on F.Cu, net +3.3V
- added copper zone on F.Cu, net +5V
- added copper zone on F.Cu, net /Power Supply/+24V_FUSED
- added copper zone on F.Cu, net /Power Supply/+5V_FUSED
- added copper zone on F.Cu, net /Power Supply/FB
- added copper zone on F.Cu, net /Power Supply/SW
- added copper zone on F.Cu, net /Power Supply/VIN
- added copper zone on F.Cu, net Net-(U3-CBOOT)
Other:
- board text added: "3V"
- board text added: "3VE"
- board text added: "5VE"
- board text removed: "3V3"
- board text removed: "3V3_EXT"
- board text removed: "5V_EXT"
- board text removed: "CAN"
